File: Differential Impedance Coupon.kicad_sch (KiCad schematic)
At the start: 3 parts, among them J1 Conn_Coaxial, J2 Conn_Coaxial

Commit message: Hook up footprint
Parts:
- J1, J2: footprint (none) -> sma_connector:SMA_142_0701_851_EdgeMount
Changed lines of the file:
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@@
       (effects (font (size 1.27 1.27)) (justify left))
     )
-    (property "Footprint" "" (at 144.78 101.6 0)
+    (property "Footprint" "sma_connector:SMA_142_0701_851_EdgeMount" (at 144.78 101.6 0)
       (effects (font (size 1.27 1.27)) hide)
     )
@@
       (effects (font (size 1.27 1.27)) (justify left))
     )
-    (property "Footprint" "" (at 144.78 86.36 0)
+    (property "Footprint" "sma_connector:SMA_142_0701_851_EdgeMount" (at 144.78 86.36 0)
       (effects (font (size 1.27 1.27)) hide)
     )

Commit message: Footprint for resistor
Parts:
- R1: footprint (none) -> Resistor_SMD:R_0805_2012Metric
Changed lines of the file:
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@@
       (effects (font (size 1.27 1.27)) (justify left))
     )
-    (property "Footprint" "" (at 169.926 94.234 90)
+    (property "Footprint" "Resistor_SMD:R_0805_2012Metric" (at 169.926 94.234 90)
       (effects (font (size 1.27 1.27)) hide)
     )

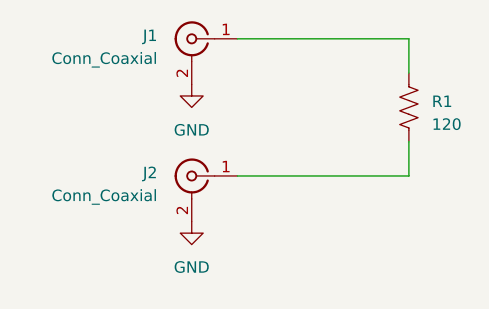
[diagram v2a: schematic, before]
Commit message: Lay out some of the traces
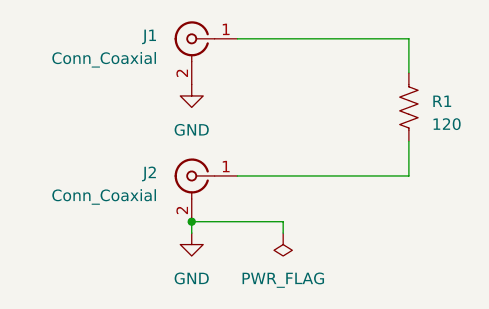
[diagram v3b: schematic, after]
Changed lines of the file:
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@@
     (rev "1.0")
   )
+  (junction (at 144.78 106.68) (diameter 0) (color 0 0 0 0)
+  )
+  (wire (pts (xy 154.94 106.68) (xy 154.94 107.95))
+    (stroke (width 0) (type default))
+  )
   (wire (pts (xy 149.86 101.6) (xy 168.91 101.6))
+    (stroke (width 0) (type default))
+  )
+  (wire (pts (xy 144.78 106.68) (xy 154.94 106.68))
     (stroke (width 0) (type default))
   )
@@
   )
   (wire (pts (xy 168.91 86.36) (xy 168.91 90.17))
+    (stroke (width 0) (type default))
+  )
+  (wire (pts (xy 144.78 107.95) (xy 144.78 106.68))
     (stroke (width 0) (type default))
   )
@@
     )
   )
+  (symbol (lib_id "power:PWR_FLAG") (at 154.94 107.95 180) (unit 1)
+    (in_bom yes) (on_board yes) (dnp no) (fields_autoplaced)
+    (property "Reference" "#FLG01" (at 154.94 109.855 0)
+      (effects (font (size 1.27 1.27)) hide)
+    )
+    (property "Value" "PWR_FLAG" (at 154.94 113.03 0)
+      (effects (font (size 1.27 1.27)))
+    )
+    (property "Footprint" "" (at 154.94 107.95 0)
+      (effects (font (size 1.27 1.27)) hide)
+    )
+    (property "Datasheet" "~" (at 154.94 107.95 0)
+      (effects (font (size 1.27 1.27)) hide)
+    )
+    (pin "1")
+    (instances
+      (project "Differential Impedance Coupon"
+        (path "/9c9bdd08-3246-4bec-8cc0-e5b6497803ef"
+          (reference "#FLG01") (unit 1)
+        )
+      )
+    )
+  )
   (symbol (lib_id "Connector:Conn_Coaxial") (at 144.78 86.36 0) (mirror y) (unit 1)
     (in_bom yes) (on_board yes) (dnp no)
@@
     )
   )
-  (symbol (lib_id "power:GND") (at 144.78 106.68 0) (unit 1)
+  (symbol (lib_id "power:GND") (at 144.78 107.95 0) (unit 1)
     (in_bom yes) (on_board yes) (dnp no) (fields_autoplaced)
-    (property "Reference" "#PWR02" (at 144.78 113.03 0)
+    (property "Reference" "#PWR02" (at 144.78 114.3 0)
       (effects (font (size 1.27 1.27)) hide)
     )
-    (property "Value" "GND" (at 144.78 111.76 0)
+    (property "Value" "GND" (at 144.78 113.03 0)
       (effects (font (size 1.27 1.27)))
     )
-    (property "Footprint" "" (at 144.78 106.68 0)
+    (property "Footprint" "" (at 144.78 107.95 0)
       (effects (font (size 1.27 1.27)) hide)
     )
-    (property "Datasheet" "" (at 144.78 106.68 0)
+    (property "Datasheet" "" (at 144.78 107.95 0)
       (effects (font (size 1.27 1.27)) hide)
     )
